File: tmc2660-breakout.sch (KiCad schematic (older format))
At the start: 18 parts, among them P1 SPI, P2 StepDir, P3 Motor, P4 VCC, P5 VMOT, U1 TMC2660

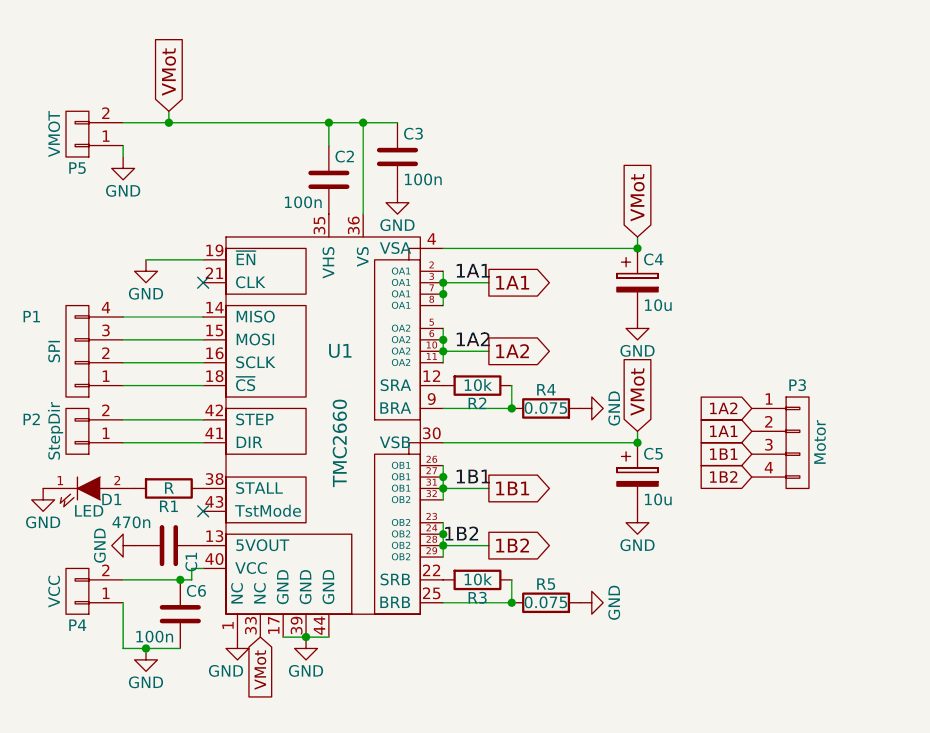
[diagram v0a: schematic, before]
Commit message: o Add alternative footprint for shunt (2512 is more appropriate)
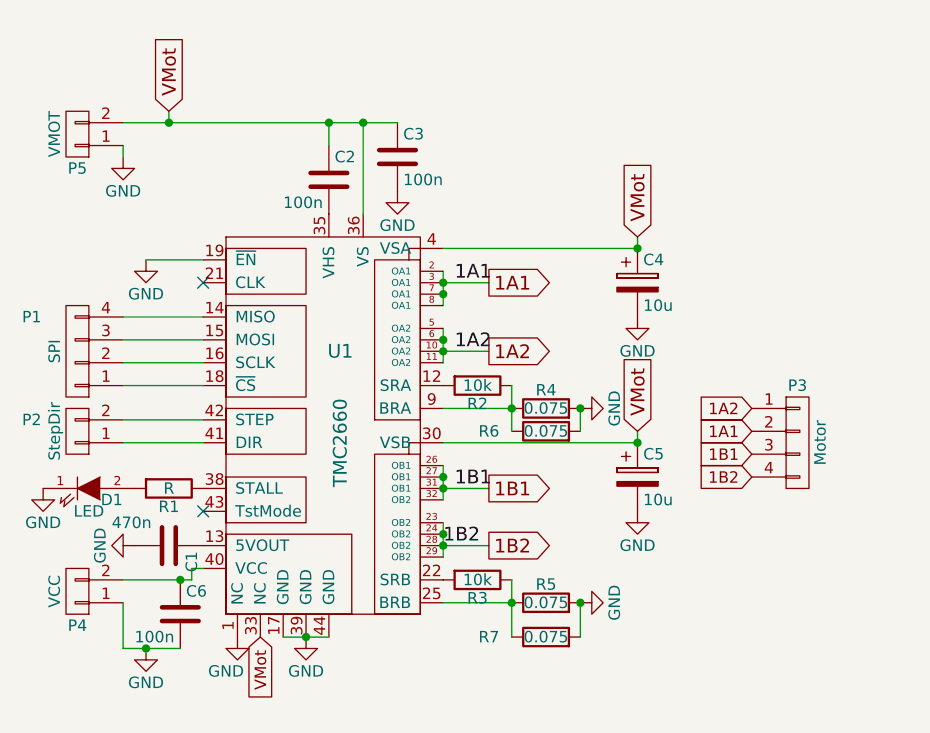
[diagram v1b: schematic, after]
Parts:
- added R6, R7: 0.075, Resistors_SMD:R_2512, symbol R
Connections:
- net GND: now also R6.2, R7.2
- net at R2.1, R4.1, U1.9 (BRA): now also R6.1
- net at R3.1, R5.1, U1.25 (BRB): now also R7.1
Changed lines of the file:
@@
 EESchema Schematic File Version 2
-LIBS:tmc2660-breakout-rescue
 LIBS:power
 LIBS:device
@@
 $EndComp
 $Comp
-L GND #PWR01
+L GND #PWR12
 U 1 1 55767A6C
 P 4800 3700
-F 0 "#PWR01" H 4800 3450 50  0001 C CNN
+F 0 "#PWR12" H 4800 3450 50  0001 C CNN
 F 1 "GND" H 4800 3550 50  0000 C CNN
 F 2 "" H 4800 3700 60  0000 C CNN
@@
 $EndComp
 $Comp
-L GND #PWR02
+L GND #PWR11
 U 1 1 55767A87
 P 4800 2850
-F 0 "#PWR02" H 4800 2600 50  0001 C CNN
+F 0 "#PWR11" H 4800 2600 50  0001 C CNN
 F 1 "GND" H 4800 2700 50  0000 C CNN
 F 2 "" H 4800 2850 60  0000 C CNN
@@
 Connection ~ 3600 2000
 $Comp
-L GND #PWR03
+L GND #PWR8
 U 1 1 55767EEE
 P 3750 2300
-F 0 "#PWR03" H 3750 2050 50  0001 C CNN
+F 0 "#PWR8" H 3750 2050 50  0001 C CNN
 F 1 "GND" H 3750 2150 50  0000 C CNN
 F 2 "" H 3750 2300 60  0000 C CNN
@@
 Connection ~ 3350 4250
 $Comp
-L GND #PWR04
+L GND #PWR7
 U 1 1 5576833D
 P 3350 4250
-F 0 "#PWR04" H 3350 4000 50  0001 C CNN
+F 0 "#PWR7" H 3350 4000 50  0001 C CNN
 F 1 "GND" H 3350 4100 50  0000 C CNN
 F 2 "" H 3350 4250 60  0000 C CNN
@@
 	3950 3250 4250 3250
 $Comp
-L GND #PWR05
+L GND #PWR9
 U 1 1 557689F4
 P 4550 3250
-F 0 "#PWR05" H 4550 3000 50  0001 C CNN
+F 0 "#PWR9" H 4550 3000 50  0001 C CNN
 F 1 "GND" H 4550 3100 50  0000 C CNN
 F 2 "" H 4550 3250 60  0000 C CNN
@@
 $EndComp
 $Comp
-L GND #PWR06
+L GND #PWR10
 U 1 1 55768AE6
 P 4550 4100
-F 0 "#PWR06" H 4550 3850 50  0001 C CNN
+F 0 "#PWR10" H 4550 3850 50  0001 C CNN
 F 1 "GND" H 4550 3950 50  0000 C CNN
 F 2 "" H 4550 4100 60  0000 C CNN
@@
 $EndComp
 $Comp
-L GND #PWR07
+L GND #PWR1
 U 1 1 55769BC1
 P 2200 3600
-F 0 "#PWR07" H 2200 3350 50  0001 C CNN
+F 0 "#PWR1" H 2200 3350 50  0001 C CNN
 F 1 "GND" H 2200 3450 50  0000 C CNN
 F 2 "" H 2200 3600 60  0000 C CNN
@@
 $EndComp
 $Comp
-L GND #PWR08
+L GND #PWR3
 U 1 1 55769FFF
 P 2600 3850
-F 0 "#PWR08" H 2600 3600 50  0001 C CNN
+F 0 "#PWR3" H 2600 3600 50  0001 C CNN
 F 1 "GND" H 2600 3700 50  0000 C CNN
 F 2 "" H 2600 3850 60  0000 C CNN
@@
 $EndComp
 Wire Wire Line
-	4250 4000 4250 4100
+	4250 4000 4250 4250
 Wire Wire Line
 	4250 4100 3950 4100
 Connection ~ 4250 4100
 Wire Wire Line
-	4250 3250 4250 3150
+	4250 3150 4250 3350
 Connection ~ 4250 3250
 Wire Wire Line
@@
 $EndComp
 $Comp
-L GND #PWR09
+L GND #PWR5
 U 1 1 56711446
 P 2650 4300
-F 0 "#PWR09" H 2650 4050 50  0001 C CNN
+F 0 "#PWR5" H 2650 4050 50  0001 C CNN
 F 1 "GND" H 2650 4150 50  0000 C CNN
 F 2 "" H 2650 4300 60  0000 C CNN
@@
 $EndComp
 $Comp
-L GND #PWR010
+L GND #PWR2
 U 1 1 5672E81A
 P 2550 2150
-F 0 "#PWR010" H 2550 1900 50  0001 C CNN
+F 0 "#PWR2" H 2550 1900 50  0001 C CNN
 F 1 "GND" H 2550 2000 50  0000 C CNN
 F 2 "" H 2550 2150 60  0000 C CNN
@@
 NoConn ~ 2900 3700
 $Comp
-L GND #PWR011
+L GND #PWR4
 U 1 1 5672F758
 P 2650 2600
-F 0 "#PWR011" H 2650 2350 50  0001 C CNN
+F 0 "#PWR4" H 2650 2350 50  0001 C CNN
 F 1 "GND" H 2650 2450 50  0000 C CNN
 F 2 "" H 2650 2600 60  0000 C CNN
@@
 VMot
 $Comp
-L GND #PWR?
+L GND #PWR6
 U 1 1 56739574
 P 3050 4250
-F 0 "#PWR?" H 3050 4000 50  0001 C CNN
+F 0 "#PWR6" H 3050 4000 50  0001 C CNN
 F 1 "GND" H 3000 4100 50  0000 C CNN
 F 2 "" H 3050 4250 60  0000 C CNN
@@
 	1    0    0    -1
 $EndComp
+$Comp
+L R R7
+U 1 1 568D6888
+P 4400 4250
+F 0 "R7" V 4400 4500 50  0000 C CNN
+F 1 "0.075" V 4400 4250 50  0000 C CNN
+F 2 "Resistors_SMD:R_2512" V 4330 4250 30  0001 C CNN
+F 3 "" H 4400 4250 30  0000 C CNN
+	1    4400 4250
+	0    -1   -1   0
+$EndComp
+Wire Wire Line
+	4550 4100 4550 4250
+Connection ~ 4550 4100
+$Comp
+L R R6
+U 1 1 568D6967
+P 4400 3350
+F 0 "R6" V 4400 3600 50  0000 C CNN
+F 1 "0.075" V 4400 3350 50  0000 C CNN
+F 2 "Resistors_SMD:R_2512" V 4330 3350 30  0001 C CNN
+F 3 "" H 4400 3350 30  0000 C CNN
+	1    4400 3350
+	0    -1   -1   0
+$EndComp
+Wire Wire Line
+	4550 3250 4550 3350
+Connection ~ 4550 3250
 $EndSCHEMATC

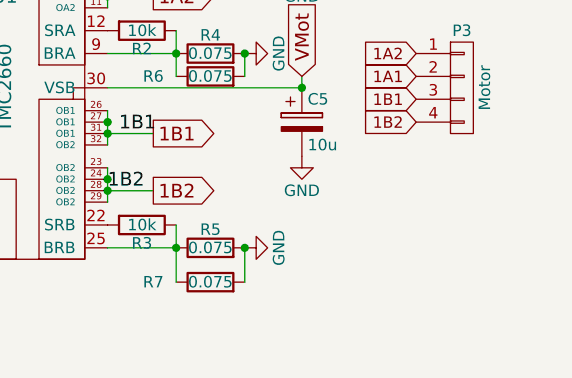
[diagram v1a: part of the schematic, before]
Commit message: o Widen the other 1206 pad to match the 2512 pad to avoid tombstoning
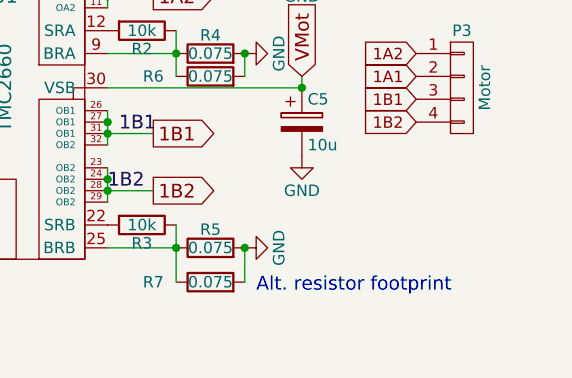
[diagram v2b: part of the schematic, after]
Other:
- note added: "Alt. resistor footprint"
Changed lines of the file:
@@
 	4550 3250 4550 3350
 Connection ~ 4550 3250
+Text Notes 4600 4300 0    60   ~ 0
+Alt. resistor footprint
 $EndSCHEMATC

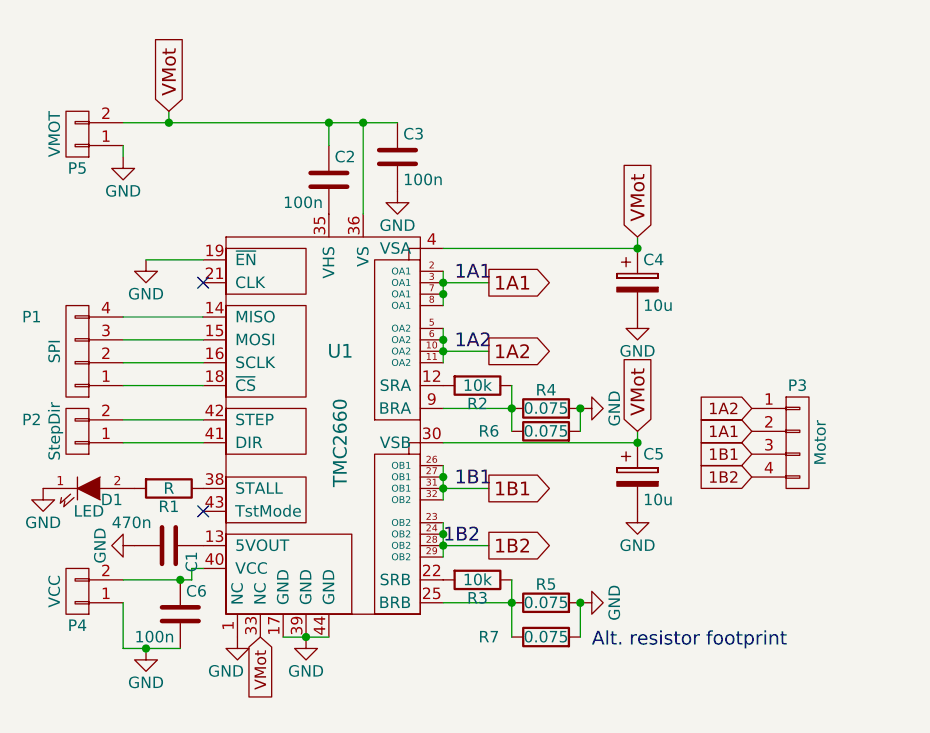
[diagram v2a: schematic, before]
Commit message: o Add optional filter caps for sense input. o Connect CLK input to GND to enable internal clock. o Fix typo in sense decoupling resistor (10k -> 10R)
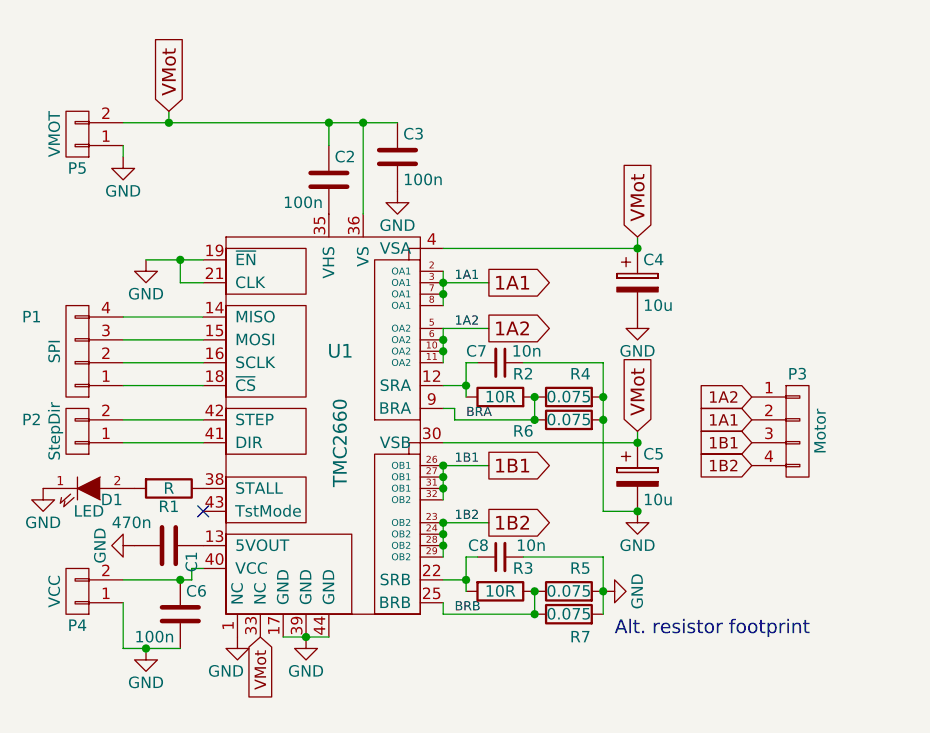
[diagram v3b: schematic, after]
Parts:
- added C7, C8: 10n, Capacitors_SMD:C_0805, symbol C_Small
- R2, R3: value 10k -> 10R
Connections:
- net GND: now also U1.21 (CLK), C7.1, C8.2
- net BRA: now reaches R4.1, R6.1, U1.9 (BRA)
- net BRA: now also R2.2; no longer R2.1
- net at U1.12 (SRA): now also R2.1, C7.2; no longer R2.2
- net BRB: now reaches R3.1, R5.1, R7.1, U1.25 (BRB)
- net at R3.2, U1.22 (SRB): now also C8.1
- no-connect marks 2 -> 1
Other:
- moved on the sheet: P3, R2, R3, R4, R5, R6, R7

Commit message: o Label some previously anonymous nets (e.g. Step/Dir).
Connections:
- net ~CS: now reaches P1.1 (P1), U1.18 (~CS)
- net SCLK: now reaches P1.2 (P2), U1.16 (SCLK)
- net MOSI: now reaches P1.3 (P3), U1.15 (MOSI)
- net MISO: now reaches P1.4 (P4), U1.14 (MISO)
- net DIR: now reaches P2.1 (P1), U1.41 (DIR)
- net STEP: now reaches P2.2 (P2), U1.42 (STEP)
- net VCC: now reaches C6.1, P4.2 (P2), U1.40 (VCC)
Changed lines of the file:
@@
 	3950 3500 4150 3500
 Connection ~ 3950 3500
+Text Label 2550 2850 0    60   ~ 0
+MISO
+Text Label 2550 2950 0    60   ~ 0
+MOSI
+Text Label 2550 3050 0    60   ~ 0
+SCLK
+Text Label 2550 3150 0    60   ~ 0
+~CS
+Text Label 2550 3300 0    60   ~ 0
+STEP
+Text Label 2550 3400 0    60   ~ 0
+DIR
+$Comp
+L VCC #PWR?
+U 1 1 5827D04F
+P 2600 4000
+F 0 "#PWR?" H 2600 3850 50  0001 C CNN
+F 1 "VCC" H 2600 3950 50  0000 C CNN
+F 2 "" H 2600 4000 50  0000 C CNN
+F 3 "" H 2600 4000 50  0000 C CNN
+	1    2600 4000
+	1    0    0    -1
+$EndComp
+Connection ~ 2600 4000
 $EndSCHEMATC

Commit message: Use current KiCAD 5.x libraries.
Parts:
- C1, C2, C3, C6: footprint Capacitors_SMD:C_0805 -> Capacitor_SMD:C_0805_2012Metric; symbol C -> Device:C
- C4, C5: footprint Capacitors_SMD:C_1206 -> Capacitor_SMD:C_1206_3216Metric; symbol CP -> Device:C
- C7, C8: footprint Capacitors_SMD:C_0805 -> Capacitor_SMD:C_0805_2012Metric; symbol C_Small -> Device:C_Small
- D1: footprint LEDs:LED-0805 -> LED_SMD:LED_0805_2012Metric; symbol LED -> Device:LED
- P1, P3: footprint Pin_Headers:Pin_Header_Straight_1x04 -> Connector_PinHeader_2.54mm:PinHeader_1x04_P2.54mm_Vertical; symbol CONN_01X04 -> Connector_Generic:Conn_01x04
- P2, P4, P5: footprint Pin_Headers:Pin_Header_Straight_1x02 -> Connector_PinHeader_2.54mm:PinHeader_1x02_P2.54mm_Vertical; symbol CONN_01X02 -> Connector_Generic:Conn_01x02
- R1, R2, R3: footprint Resistors_SMD:R_0805 -> Resistor_SMD:R_0805_2012Metric; symbol R -> Device:R
- R4, R5: footprint Resistors_SMD:R_1206 -> Resistor_SMD:R_1206_3216Metric; symbol R -> Device:R
- R6, R7: footprint Resistors_SMD:R_2512 -> Resistor_SMD:R_2512_6332Metric; symbol R -> Device:R
- U1: footprint Housings_QFP:LQFP-44_10x10mm_Pitch0.8mm -> Package_QFP:LQFP-44_10x10mm_P0.8mm; symbol TMC2660 -> tmc2660:TMC2660
